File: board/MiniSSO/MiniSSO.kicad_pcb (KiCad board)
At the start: 2 copper layers, 50.8 x 22.9 mm, 35 parts, among them J1 Conn_01x02, J2 Conn_01x02, J3 Conn_01x16, J4 Conn_01x03, J5 Conn_01x12, Q1 MCU30N02-TP, Q2 MCU30N02-TP, SW1 SW_Push, U2 LTV-356T

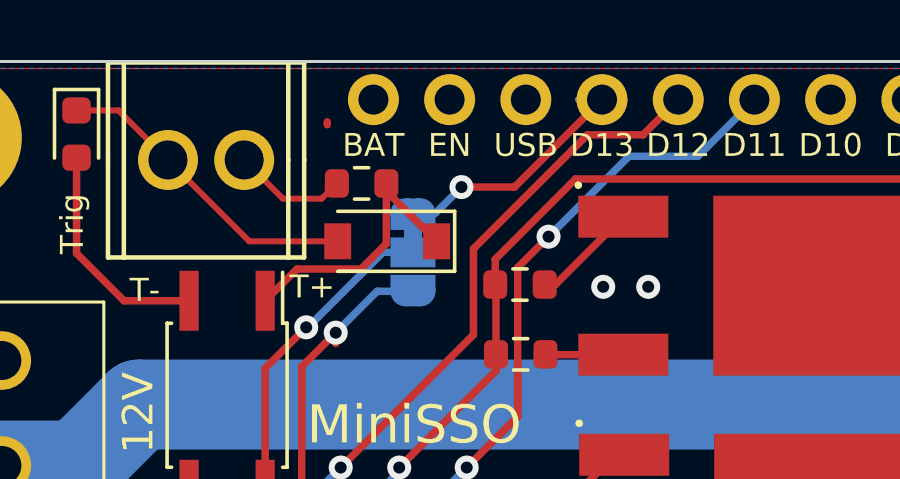
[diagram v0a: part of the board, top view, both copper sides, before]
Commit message: Rev 1: Modified trace to solder bridge for input to provide larger ground plane around the solder bridge.
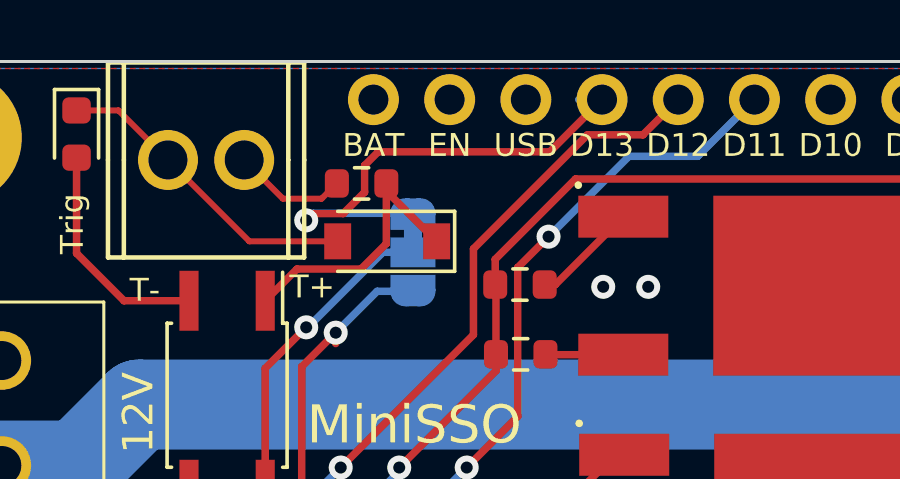
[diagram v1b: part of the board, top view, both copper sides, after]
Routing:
- net /D13: track 8.65 -> 16.5 mm
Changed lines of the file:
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@@
     (style (thickness 0.15) (arrow_length 1.27) (text_position_mode 0) (extension_height 0.58642) (extension_offset 0.5) keep_text_aligned)
   )
-  (segment (start 131.8 71.5) (end 131.8 71.6) (width 0.25) (layer "F.Cu") (net 0))
   (segment (start 133.771525 73.553269) (end 133.771525 75.559091) (width 0.25) (layer "F.Cu") (net 1))
   (segment (start 133.771525 73.807269) (end 133.771525 73.553269) (width 0.25) (layer "F.Cu") (net 1))
@@
   (segment (start 124.714 88.074) (end 124.714 90.072544) (width 0.25) (layer "F.Cu") (net 16))
   (segment (start 128.260725 91.079269) (end 125.720725 91.079269) (width 0.45) (layer "F.Cu") (net 16))
-  (segment (start 136.275 73.675) (end 138.044994 73.675) (width 0.25) (layer "F.Cu") (net 21))
-  (segment (start 138.044994 73.675) (end 140.960725 70.759269) (width 0.25) (layer "F.Cu") (net 21))
-  (via (at 136.275 73.675) (size 0.8) (drill 0.4) (layers "F.Cu" "B.Cu") (net 21))
-  (segment (start 134.6575 74.55) (end 135.4 74.55) (width 0.25) (layer "B.Cu") (net 21))
+  (segment (start 133.047005 73.844572) (end 133.047005 72.952995) (width 0.25) (layer "F.Cu") (net 21))
+  (segment (start 133.047005 72.952995) (end 133.5 72.5) (width 0.25) (layer "F.Cu") (net 21))
+  (segment (start 139.219994 72.5) (end 140.960725 70.759269) (width 0.25) (layer "F.Cu") (net 21))
+  (segment (start 132.332419 74.559158) (end 133.047005 73.844572) (width 0.25) (layer "F.Cu") (net 21))
+  (segment (start 133.5 72.5) (end 139.219994 72.5) (width 0.25) (layer "F.Cu") (net 21))
+  (segment (start 131.1 74.784169) (end 131.325011 74.559158) (width 0.25) (layer "F.Cu") (net 21))
+  (segment (start 131.325011 74.559158) (end 132.332419 74.559158) (width 0.25) (layer "F.Cu") (net 21))
+  (via (at 131.1 74.784169) (size 0.8) (drill 0.4) (layers "F.Cu" "B.Cu") (net 21))
+  (segment (start 131.334169 74.55) (end 131.1 74.784169) (width 0.25) (layer "B.Cu") (net 21))
   (segment (start 140.183587 70.759269) (end 140.960725 70.759269) (width 0.25) (layer "B.Cu") (net 21))
-  (segment (start 135.4 74.55) (end 136.275 73.675) (width 0.25) (layer "B.Cu") (net 21))
+  (segment (start 134.6575 74.55) (end 131.334169 74.55) (width 0.25) (layer "B.Cu") (net 21))
   (segment (start 136.675 75.733006) (end 140.474226 71.93378) (width 0.25) (layer "F.Cu") (net 22))
   (segment (start 132.25 83.0239) (end 136.675 78.5989) (width 0.25) (layer "F.Cu") (net 22))

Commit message: Revision 2. First production board run.
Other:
- board text added: "Output 1"
- board text added: "Rev 2"
- board text removed: "Rev 1"
